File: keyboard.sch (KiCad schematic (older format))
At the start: 84 parts, among them IC1 ATMEGA32U4, J1 MINI, P1 CONN_1, P10 CONN_1, P11 CONN_1, P12 CONN_1, P13 CONN_1, P14 CONN_1, P15 CONN_1, P16 CONN_1, P17 CONN_1, P18 CONN_1, P19 CONN_1, P2 CONN_1, P20 CONN_1, P21 CONN_1, P22 CONN_1, P23 CONN_1, P24 CONN_1, P25 CONN_1, P26 CONN_1, P27 CONN_1, P28 CONN_1, P29 CONN_1, P3 CONN_1, P30 CONN_1, P31 CONN_1, P32 CONN_1, P33 CONN_1, P34 CONN_1, P35 CONN_1, P36 CONN_1, P37 CONN_1, P38 CONN_1, P39 CONN_1, P4 CONN_1, P40 CONN_1, P41 CONN_1, P42 CONN_1, P5 CONN_1, P6 CONN_1, P7 CONN_1, P8 CONN_1, P9 CONN_1, X1 ASX3F

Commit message: remap symbols.
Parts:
- C1, C2, C3, C4, C5, C6, C7, C8: symbol C -> device:C
- DF10, DF11, DF20, DF201, DF21, DF211, DF22, DF221, DF23, DF231, DF232, DF3, DW1, DW2, DW3, DW4: symbol LED -> device:LED
- IC1: symbol ATMEGA32U4 -> atmega32u4:ATMEGA32U4
- J1: symbol USBMINI_B05 -> oupiin_usb:USBMINI_B05
- P1, P10, P11, P12, P13, P14, P15, P16, P17, P18, P19, P2, P20, P21, P22, P23, P24, P25, P26, P27, P28, P29, P3, P30, P31, P32, P33, P34, P35, P36, P37, P38, P39, P4, P40, P41, P42, P5, P6, P7, P8, P9: symbol CONN_1 -> conn:CONN_1
- R1, R10, R11, R12, R13, R14, R15, R2, R3, R5, R6, R7, R8, R9: symbol R -> device:R
- S0: symbol DTSM-6 -> dtsjw:DTSM-6
- X1: symbol ASX4 -> aker:ASX4
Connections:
- wire segments 205 -> 245

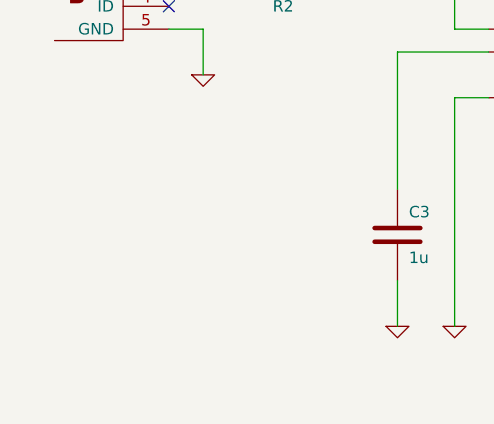
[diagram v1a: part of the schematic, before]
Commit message: add pwr_flag to gnd.
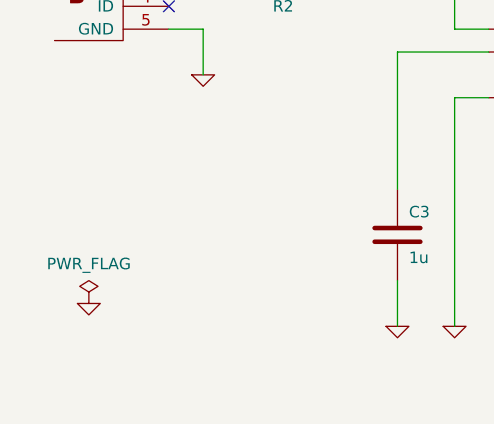
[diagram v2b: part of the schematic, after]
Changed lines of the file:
@@
 Wire Bus Line
 	6550 2950 6550 6500
+$Comp
+L power1:GND #PWR0101
+U 1 1 5D172B2C
+P 1000 7250
+F 0 "#PWR0101" H 1000 7250 30  0001 C CNN
+F 1 "GND" H 1000 7180 30  0001 C CNN
+F 2 "" H 1000 7250 60  0001 C CNN
+F 3 "" H 1000 7250 60  0001 C CNN
+	1    1000 7250
+	1    0    0    -1
+$EndComp
+$Comp
+L power:PWR_FLAG #FLG0101
+U 1 1 5D1739C3
+P 1000 7250
+F 0 "#FLG0101" H 1000 7325 50  0001 C CNN
+F 1 "PWR_FLAG" H 1000 7423 50  0000 C CNN
+F 2 "" H 1000 7250 50  0001 C CNN
+F 3 "~" H 1000 7250 50  0001 C CNN
+	1    1000 7250
+	1    0    0    -1
+$EndComp
 $EndSCHEMATC

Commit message: assign footprints.
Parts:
- DF21, DF211, DF22, DF221, DF23, DF231, DF232: footprint (none) -> mx1a:MX1A-led
- P1, P10, P11, P12, P13, P14, P15, P16, P17, P18, P19, P2, P20, P21, P22, P23, P24, P25, P26, P27, P28, P29, P3, P30, P31, P32, P33, P34, P35, P36, P37, P38, P39, P4, P40, P41, P42, P5, P6, P7, P8, P9: footprint (none) -> pad:pad
- R10, R11, R12, R13, R14, R15, R6, R7, R8, R9: footprint (none) -> res:resistor
